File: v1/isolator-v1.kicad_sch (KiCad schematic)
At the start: 12 parts, among them J1 HOST, U1 ADuM4165, U2 USBLC6-2SC6, Y1 24M 8pF

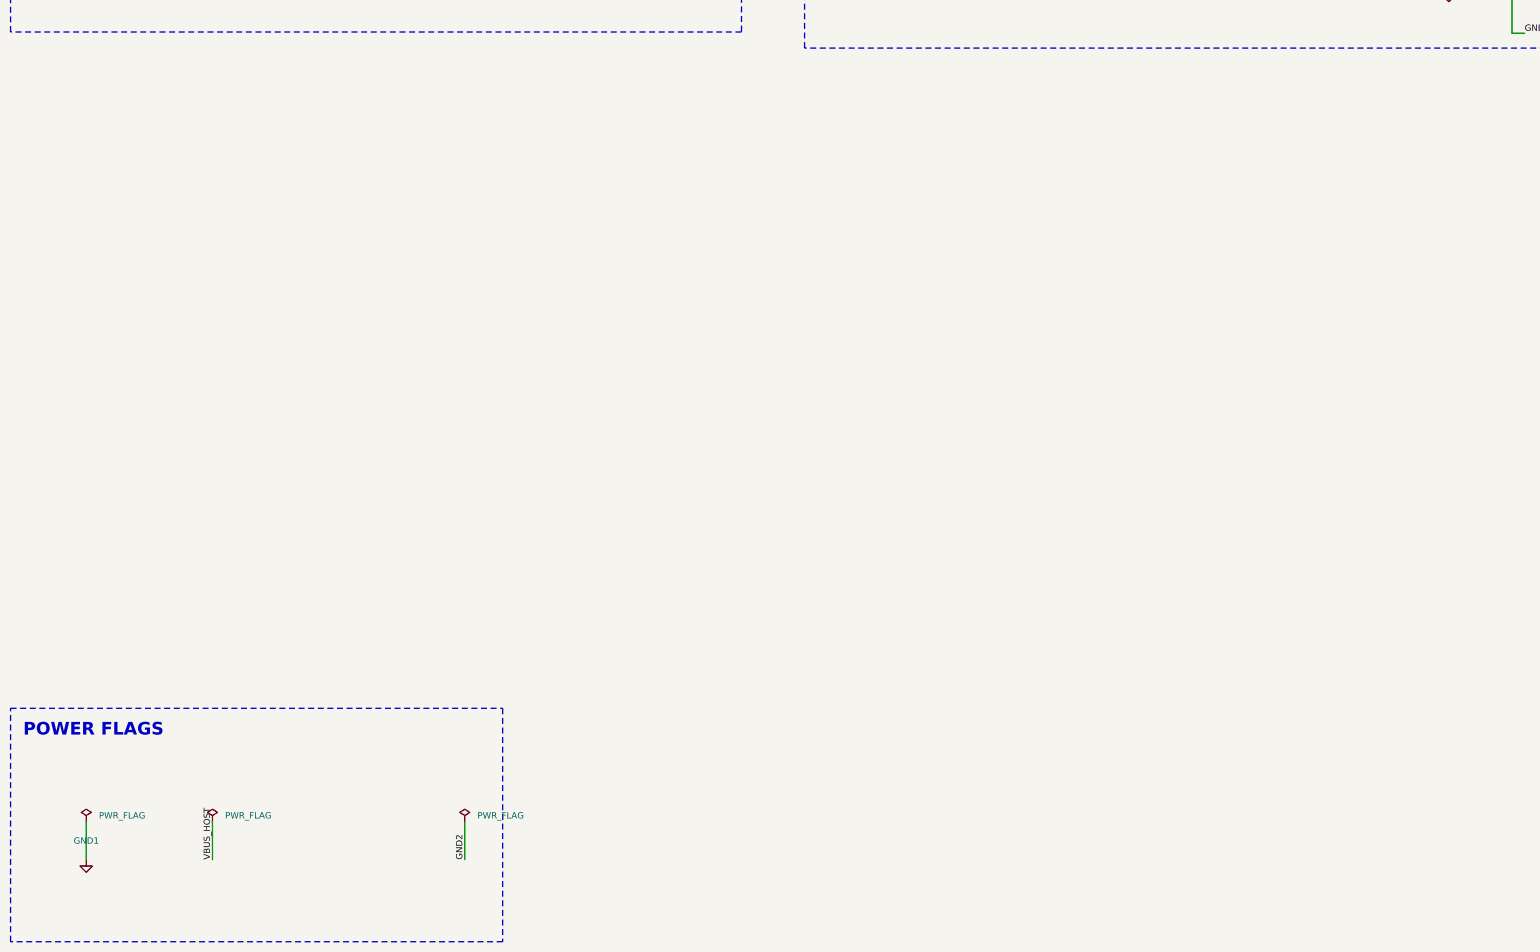
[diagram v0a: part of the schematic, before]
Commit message: feat(v1/sch): SN6505B isolated DC-DC, full-wave rectifier, 5V LDO
Adds Task 4's isolated power section to v1/isolator-v1.kicad_sch: U4
(SN6505BDBV push-pull driver), T1 (750313638 transformer), D1/D2 (SS34
full-wave center-tap rectifier), U5 (TLV76750DGNR 5.0V LDO), and their
associated bypass/bulk capacitors (C6-C11), producing the DCDC_RAW,
ISO_5V, and GND2 nets. Topology transcribed verbatim from the reviewed
v2 design; TLV76750DGNR pinout (including SNS-to-OUT tie and thermal
pad to GND2) verified against the TI datasheet.

ERC: 0 errors (severity-error gate), 1 pre-existing informational
warning inherited unavoidably from copying v2's own embedded
SN6505BDBV symbol (confirmed identical warning already present in
v2's own ERC output). Isolation check confirms GND1/GND2 are bridged
only by U1 and T1, as required. VBUS_HOST bulk capacitance: 9.6 uF,
under the USB 2.0 10 uF bus-powered limit.

Co-Authored-By: Claude Opus 5 <noreply@anthropic.com>
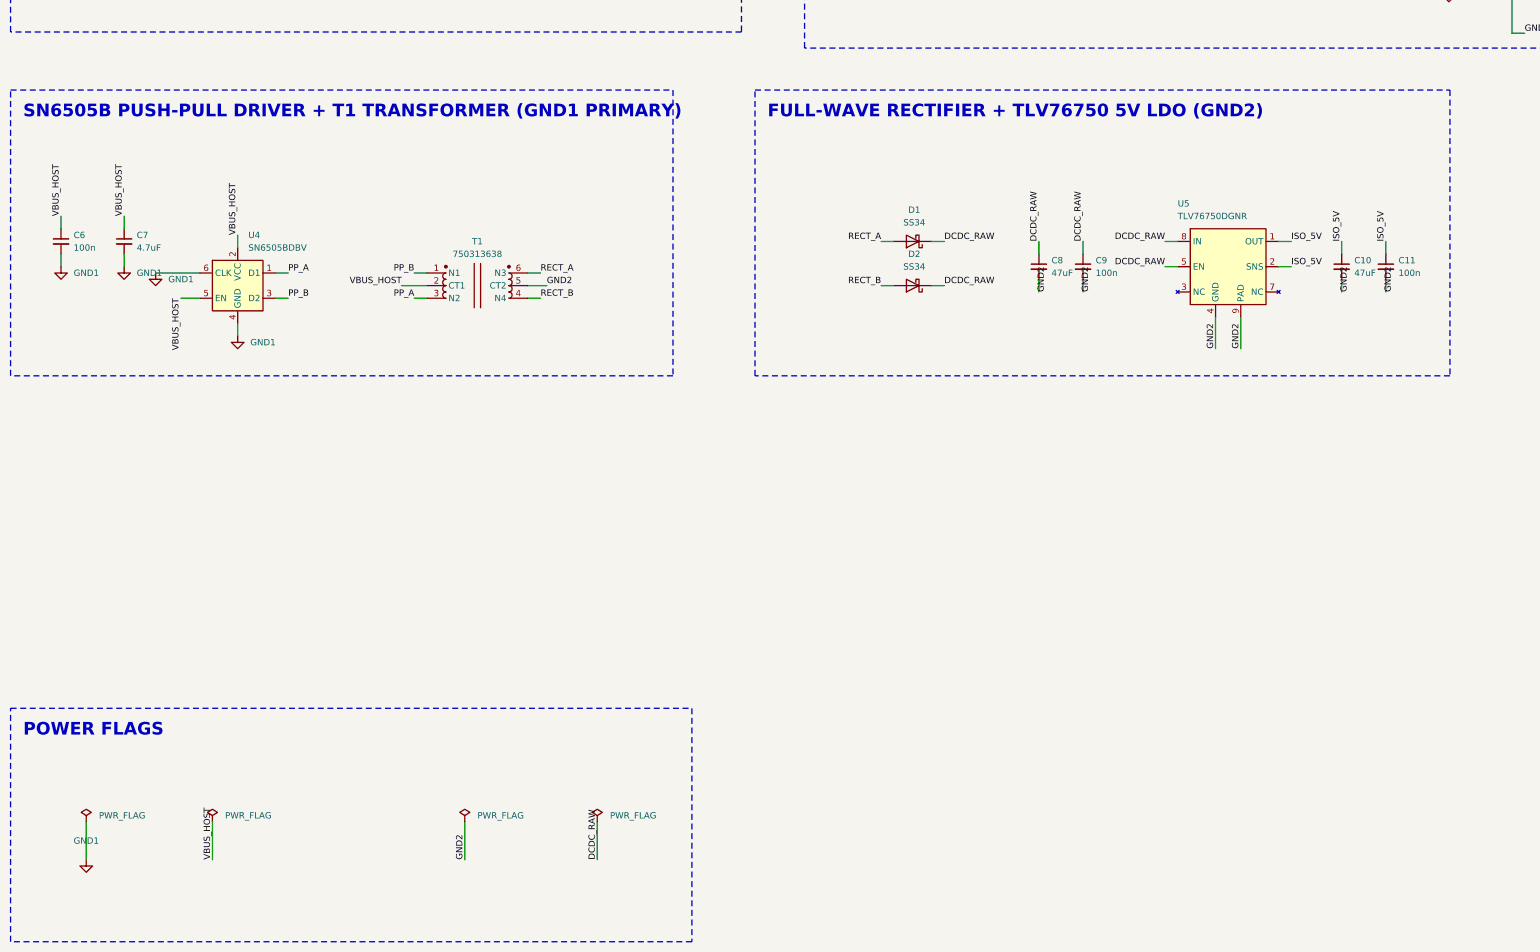
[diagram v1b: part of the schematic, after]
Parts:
- added C10, C8: 47uF, Capacitor_SMD:C_1210_3225Metric, symbol Device:C_Small
- added C11, C6, C9: 100n, Capacitor_SMD:C_0603_1608Metric, symbol Device:C_Small
- added C7: 4.7uF, Capacitor_SMD:C_0805_2012Metric, symbol Device:C_Small
- added D1, D2: SS34, Diode_SMD:D_SMA, symbol Device:D_Schottky
- added T1: 750313638, isolator-lib:WE_750313638, symbol isolator-lib:750313638
- added U4: SN6505BDBV, Package_TO_SOT_SMD:SOT-23-6, symbol Power_Management:SN6505BDBV
- added U5: TLV76750DGNR, Package_SO:HVSSOP-8-1EP_3x3mm_P0.65mm_EP1.57x1.89mm, symbol isolator-lib:TLV76750DGNR
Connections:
- net GND1: now also C6.2, C7.2, U4.4 (GND), U4.6 (CLK)
- net GND2: now also C10.2, C11.2, C8.2, C9.2, T1.5 (CT2), U5.4 (GND), U5.6 (GND), U5.9 (PAD)
- net VBUS_HOST: now also C6.1, C7.1, T1.2 (CT1), U4.2 (VCC), U4.5 (EN)
- new net DCDC_RAW: C8.1, C9.1, D1.1 (K), D2.1 (K), U5.5 (EN), U5.8 (IN)
- new net ISO_5V: C10.1, C11.1, U5.1 (OUT), U5.2 (SNS)
- new net PP_A: T1.3 (N2), U4.1 (D1)
- new net PP_B: T1.1 (N1), U4.3 (D2)
- new net RECT_A: D1.2 (A), T1.6 (N3)
- new net RECT_B: D2.2 (A), T1.4 (N4)
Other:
- note added: "FULL-WAVE RECTIFIER + TLV76750 5V LDO (GND2)"
- note added: "SN6505B PUSH-PULL DRIVER + T1 TRANSFORMER (GND1 PRIMARY)"

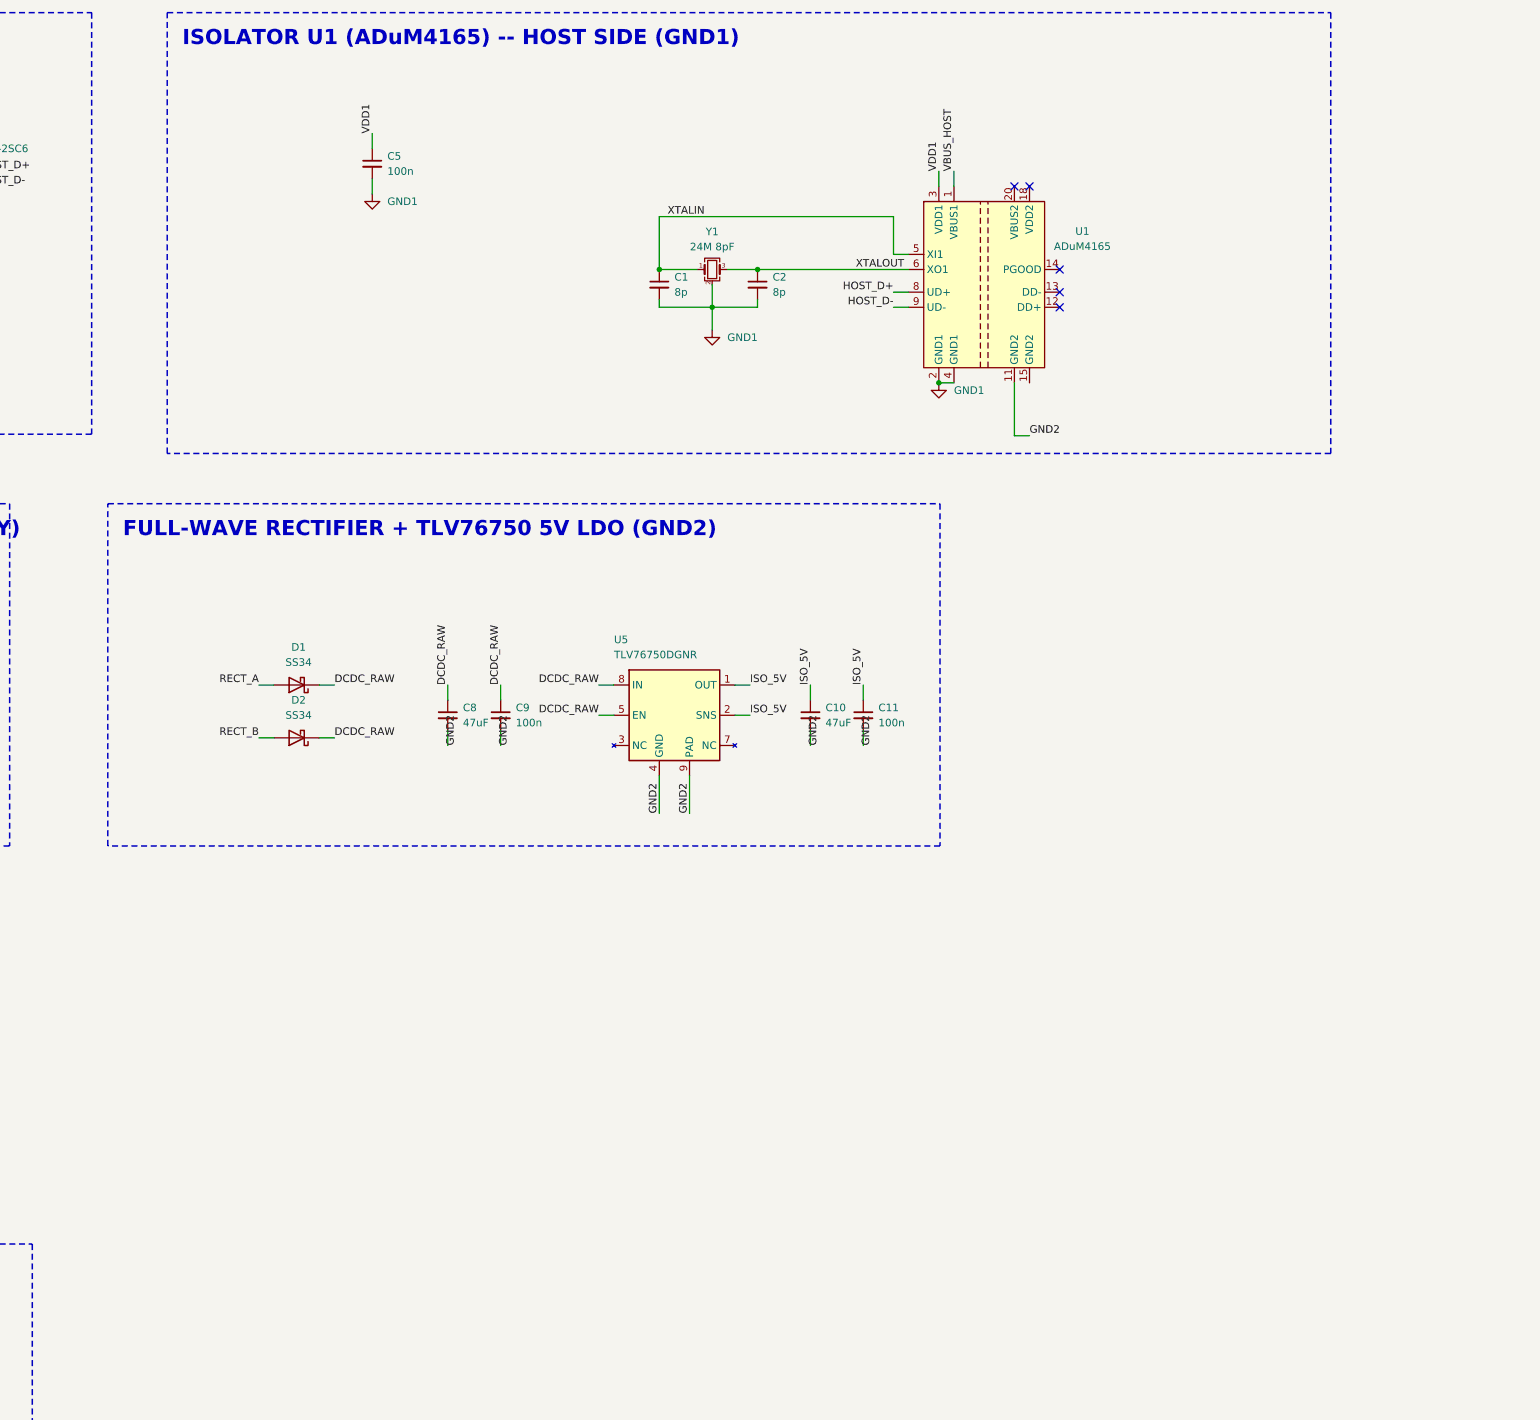
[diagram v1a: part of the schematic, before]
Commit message: feat(v1/sch): ADuM Side 2, TPS2553 port switch, downstream USB-C
Wires the isolated (GND2) output side of the v1 USB isolator - the last
electrical task. ADuM4165 U1 Side-2 pins (DD+/DD-/PGOOD/VDD2/VBUS2) are
now live; TPS2553DBV (U6) current-limited port switch, USBLC6-2SC6 (U3)
ESD protection, T6V0S5A-7 (D6) VBUS TVS, PGOOD/FAULT LED indicators
(D3/D4), and the downstream USB-C receptacle (J2) are placed and wired.

Four datasheet-driven decisions, each independently verified rather than
assumed or copied:
- D6 TVS polarity re-derived from the Diodes Inc. datasheet's own device
  schematic diagram (pin1=cathode->PORT_VBUS, pin2=anode->GND2) rather
  than copied from D5's wiring, per the review-round-1 lesson from D5.
- ADuM4165 PGOOD is push-pull (no external pull-up drawn in the
  datasheet's own application diagram, no open-drain language anywhere
  in the doc) -> D3 wired PGOOD2 -> LED -> 1.3k -> GND2, no transistor
  needed.
- TPS2553 ILIM resistor solved from the datasheet's IOS(min) equation
  (the "design above a minimum threshold" case, matching how v2's own
  40.2k/~600mA was actually derived) for I_OS=250mA -> R3=93.1k.
- VDD2 retyped power_in->power_out, verified for Side 2 specifically
  from the Power Supply Options section (VBUS2 fed from ISO_5V is a
  genuine LDO input) - and its suspend-mode rise to ~5V is exactly why
  C13 is the only thing on that net.

Isolation check clean (GND1/GND2 domains only bridge at U1/T1, as
before); PORT_D+/PORT_D-/PORT_CC1/PORT_CC2/VDD2 all contain exactly the
expected nodes. ERC: 0 errors, same single pre-existing lib_symbol_mismatch
warning as Task 4 (no new warnings).

Co-Authored-By: Claude Opus 5 <noreply@anthropic.com>
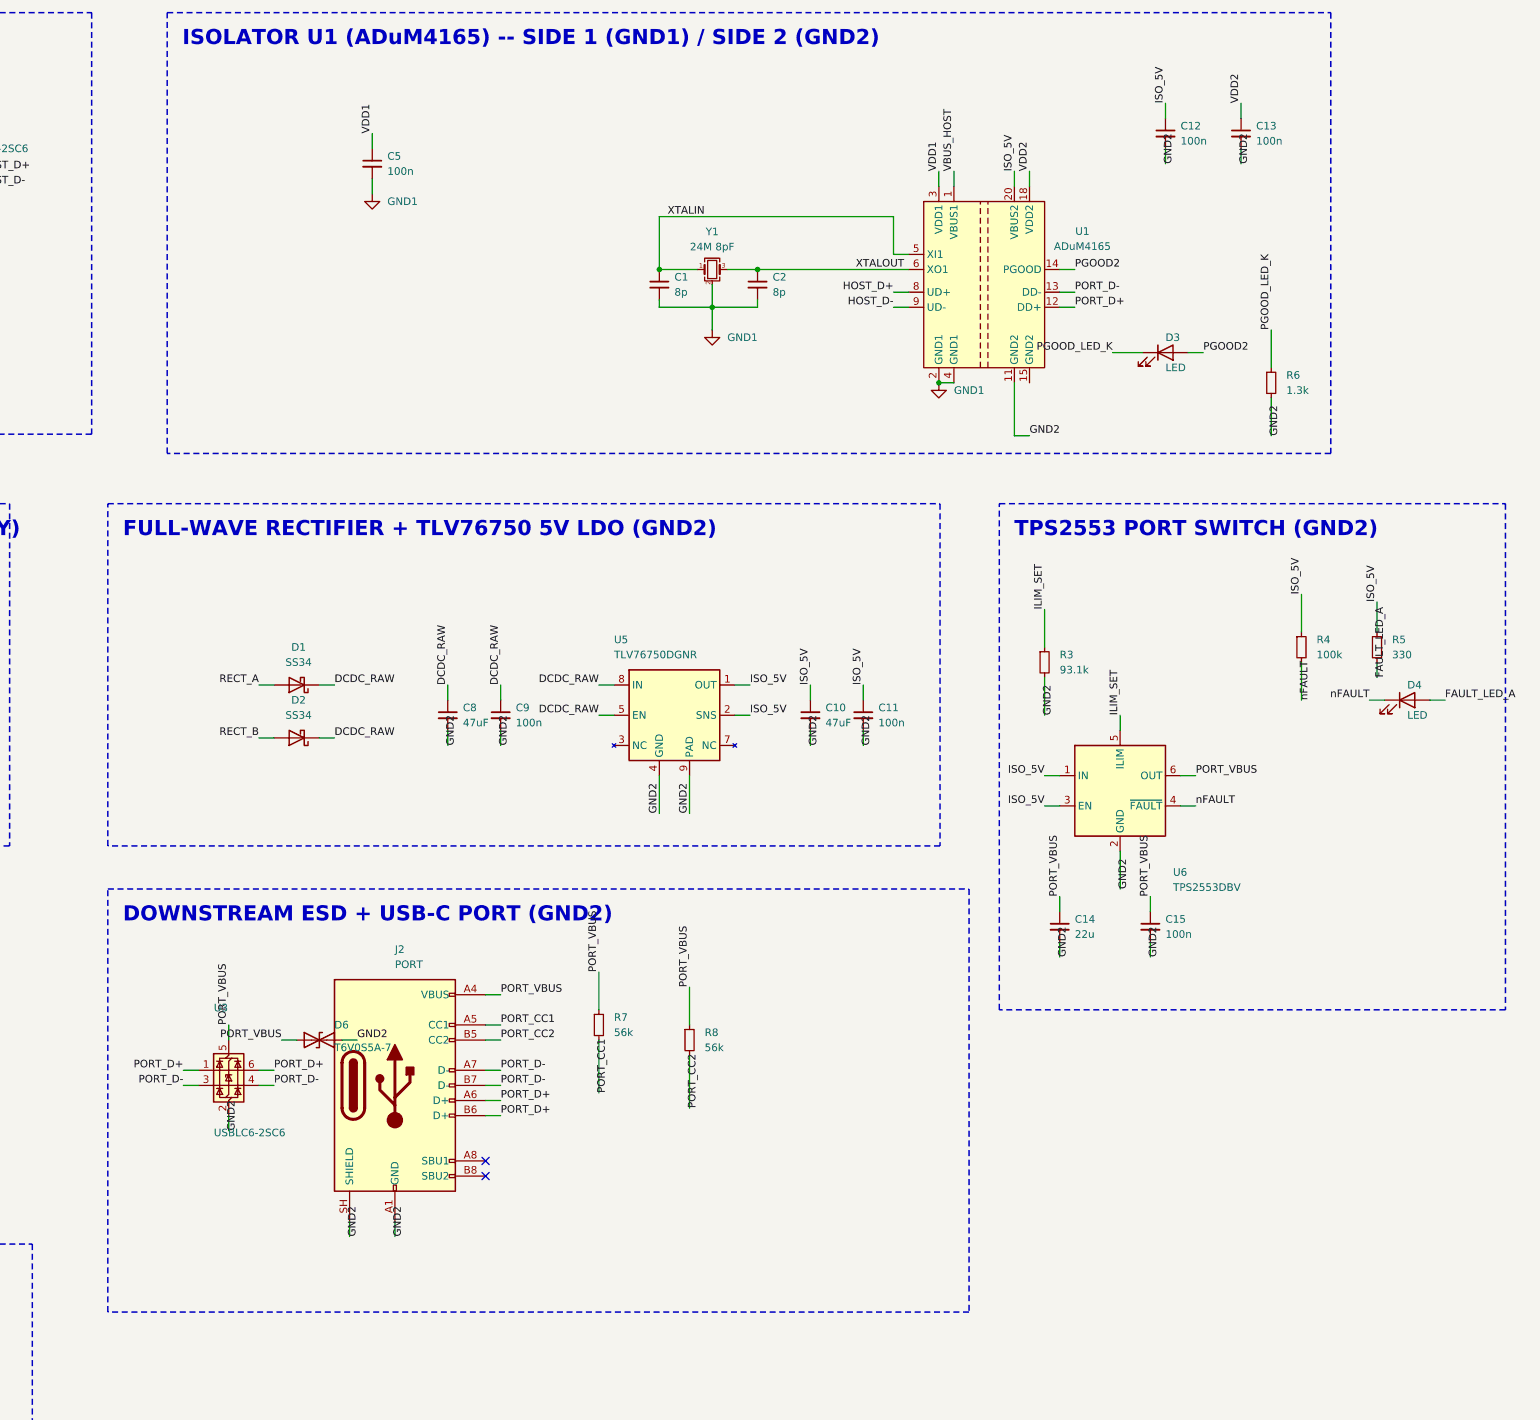
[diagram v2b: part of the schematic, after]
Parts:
- added C12, C13, C15: 100n, Capacitor_SMD:C_0603_1608Metric, symbol Device:C_Small
- added C14: 22u, Capacitor_SMD:C_0805_2012Metric, symbol Device:C_Small
- added D3, D4: LED, LED_SMD:LED_0603_1608Metric, symbol Device:LED
- added D6: T6V0S5A-7, Diode_SMD:D_SOD-523, symbol Device:D_TVS
- added J2: PORT, Connector_USB:USB_C_Receptacle_HRO_TYPE-C-31-M-12, symbol Connector:USB_C_Receptacle_USB2.0_16P
- added R3: 93.1k, Resistor_SMD:R_0603_1608Metric, symbol Device:R_Small
- added R4: 100k, Resistor_SMD:R_0603_1608Metric, symbol Device:R_Small
- added R5: 330, Resistor_SMD:R_0603_1608Metric, symbol Device:R_Small
- added R6: 1.3k, Resistor_SMD:R_0603_1608Metric, symbol Device:R_Small
- added R7, R8: 56k, Resistor_SMD:R_0603_1608Metric, symbol Device:R_Small
- added U3: USBLC6-2SC6, Package_TO_SOT_SMD:SOT-23-6, symbol Power_Protection:USBLC6-2SC6
- added U6: TPS2553DBV, Package_TO_SOT_SMD:SOT-23-6, symbol isolator-lib:TPS2553DBV
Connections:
- net GND2: now also C12.2, C13.2, C14.2, C15.2, D6.2 (A2), J2.A1 (GND), J2.A12 (GND), J2.B1 (GND), J2.B12 (GND), J2.SH (SHIELD), R3.2, R6.2, U3.2 (GND), U6.2 (GND)
- net ISO_5V: now also U1.20 (VBUS2), C12.1, R4.1, R5.1, U6.1 (IN), U6.3 (EN)
- net PORT_D+: now reaches U1.12 (DD+)
- net PORT_D+: now also J2.A6 (D+), J2.B6 (D+), U3.1 (I/O1), U3.6 (I/O1)
- net PORT_D-: now reaches U1.13 (DD-)
- net PORT_D-: now also J2.A7 (D-), J2.B7 (D-), U3.3 (I/O2), U3.4 (I/O2)
- net PGOOD2: now reaches U1.14 (PGOOD)
- net PGOOD2: now also D3.2 (A)
- net VDD2: now reaches U1.18 (VDD2)
- net VDD2: now also C13.1
- new net FAULT_LED_A: D4.2 (A), R5.2
- new net ILIM_SET: R3.1, U6.5 (ILIM)
- new net PGOOD_LED_K: D3.1 (K), R6.1
- new net PORT_CC1: J2.A5 (CC1), R7.2
- new net PORT_CC2: J2.B5 (CC2), R8.2
- new net PORT_VBUS: C14.1, C15.1, D6.1 (A1), J2.A4 (VBUS), J2.A9 (VBUS), J2.B4 (VBUS), J2.B9 (VBUS), R7.1, R8.1, U3.5 (VBUS), U6.6 (OUT)
- new net nFAULT: D4.1 (K), R4.2, U6.4 (~{FAULT})
- no-connect marks 7 -> 4
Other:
- note added: "DOWNSTREAM ESD + USB-C PORT (GND2)"
- note added: "ISOLATOR U1 (ADuM4165) -- SIDE 1 (GND1) / SIDE 2 (GND2)"
- note added: "TPS2553 PORT SWITCH (GND2)"
- note removed: "ISOLATOR U1 (ADuM4165) -- HOST SIDE (GND1)"
